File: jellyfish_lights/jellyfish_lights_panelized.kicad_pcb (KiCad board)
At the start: 2 copper layers, 162.8 x 143.6 mm, 424 parts, among them Q1 AO3400A, SW1 tilt switch, U1 SN74LVC1G14DBV

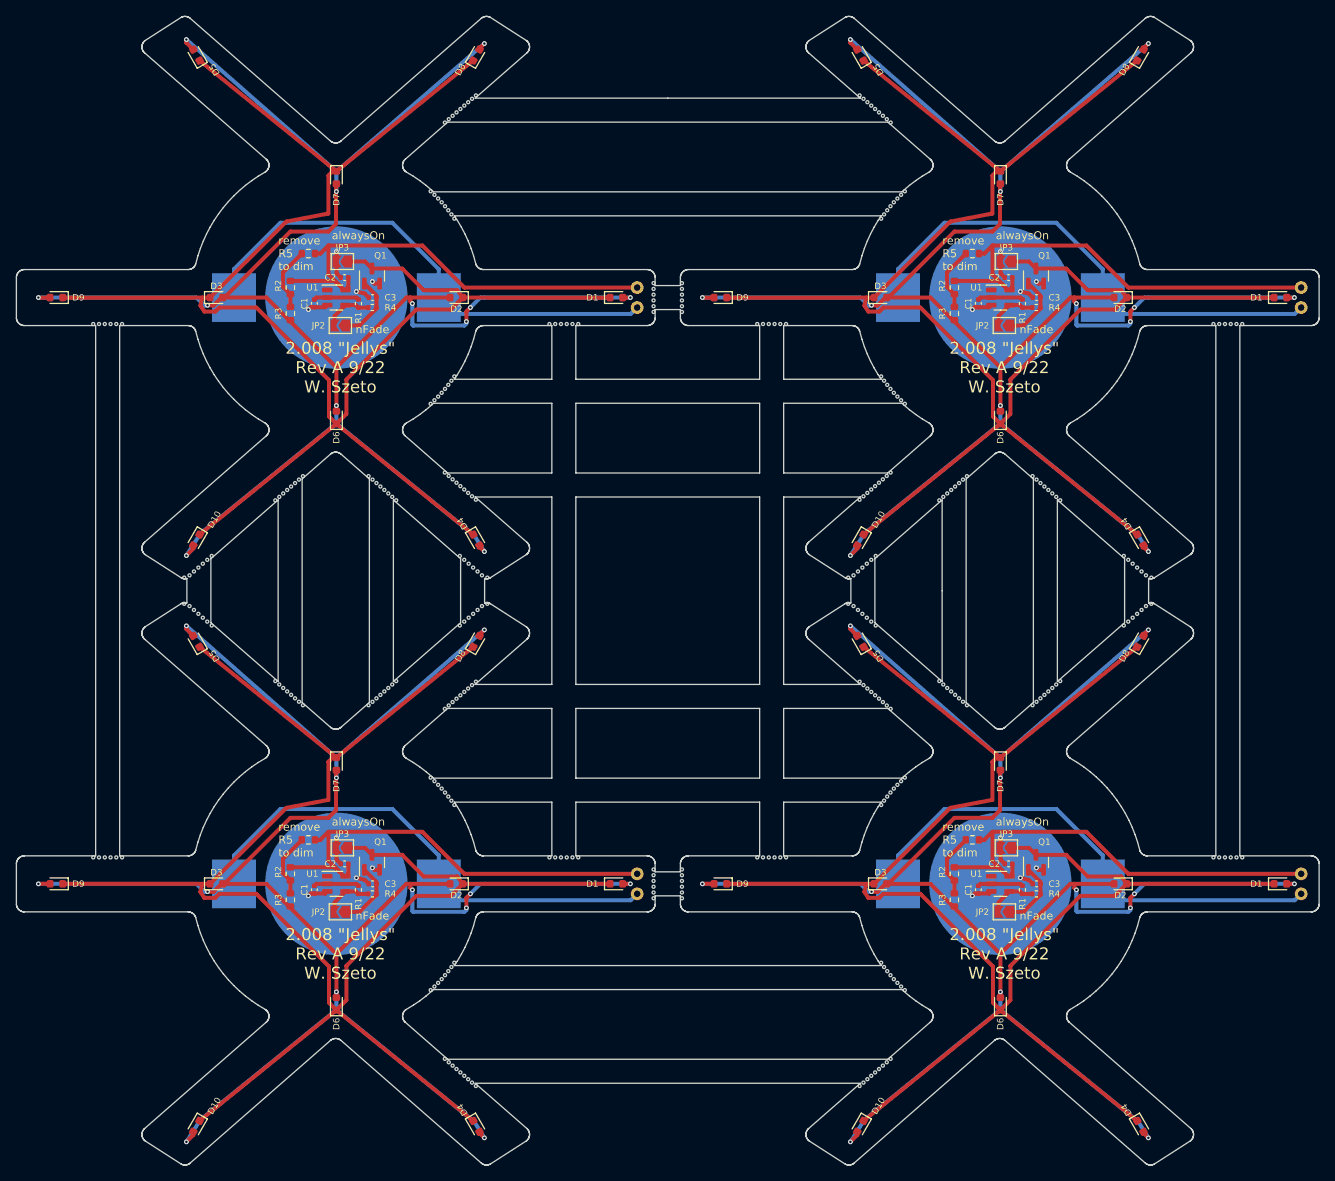
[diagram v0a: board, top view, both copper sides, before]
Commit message: created B01
B01 has a new circuit to do blinking. The op-amp allows for fading of the lights
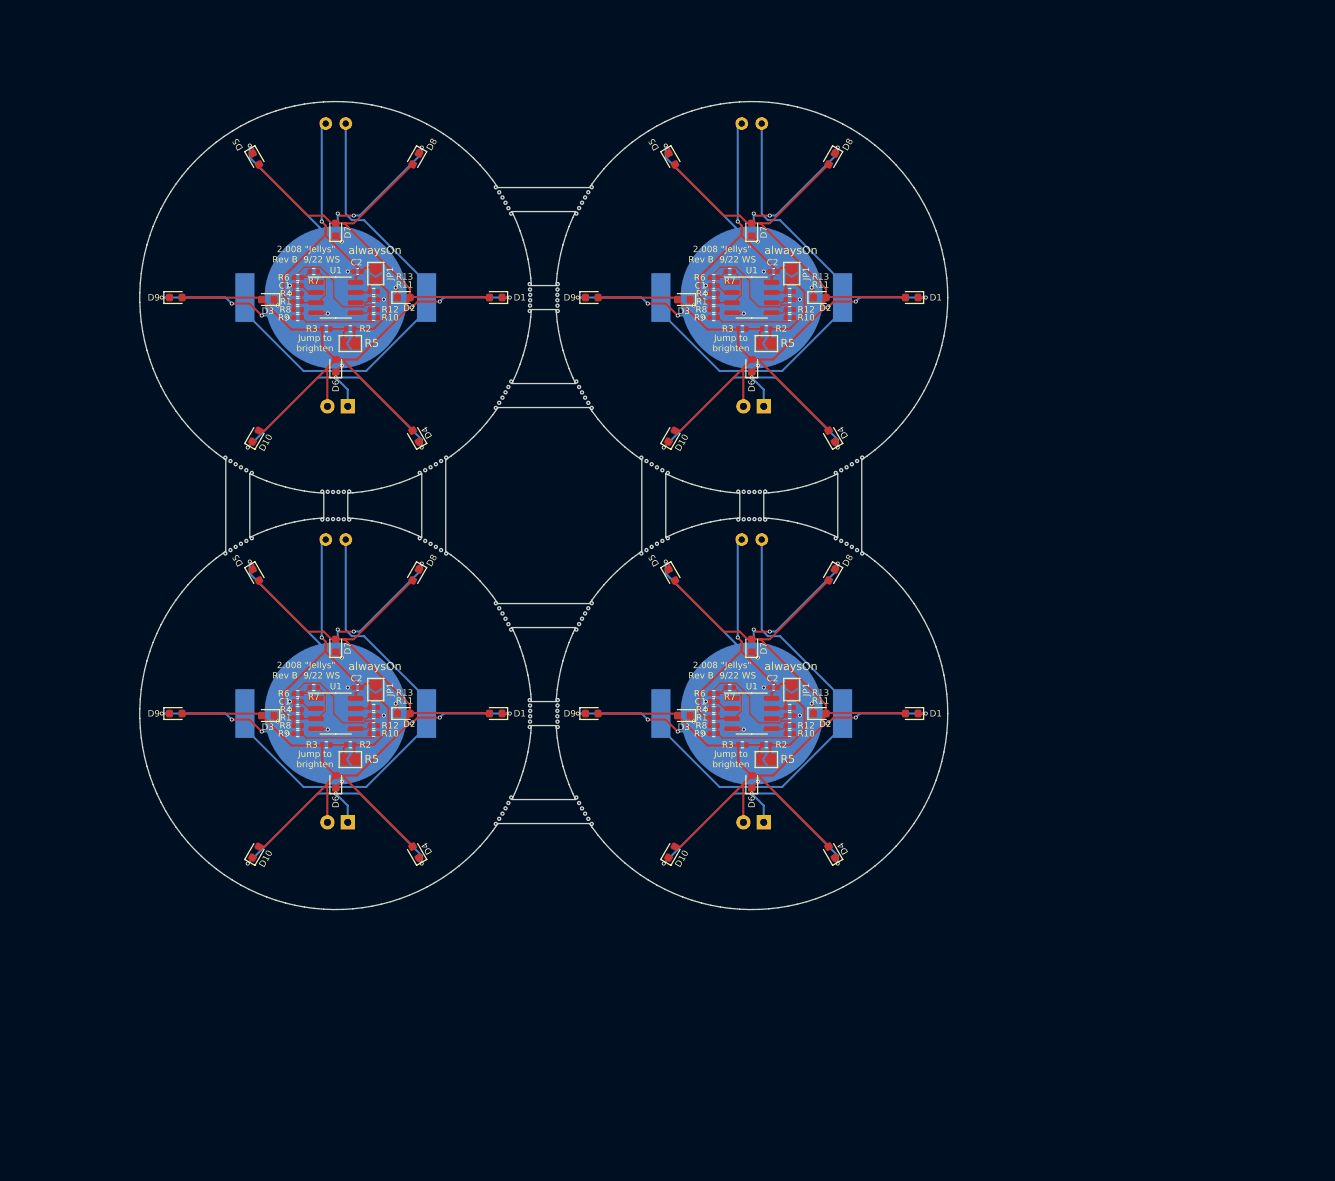
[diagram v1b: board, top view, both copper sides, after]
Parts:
- removed the BT1 at (50.1, 50.0)
- removed the BT1 at (133.1, 123.3)
- removed the BT1 at (133.1, 50.0)
- removed the BT1 at (50.1, 123.3)
- removed the C1 at (47.3, 50.7)
- removed the C1 at (130.3, 50.7)
- removed the C1 at (130.3, 124.0)
- removed the C1 at (47.3, 124.0)
- removed the C2 at (51.1, 120.8)
- removed the C2 at (134.1, 120.8)
- removed the C2 at (134.1, 47.5)
- removed the C2 at (51.1, 47.5)
- removed C3 (x4): 1uF, Capacitor_SMD:C_0402_1005Metric
- removed the D1 at (85.1, 123.3)
- removed the D1 at (168.1, 50.0)
- removed the D1 at (85.1, 50.0)
- removed the D1 at (168.1, 123.3)
- removed the D10 at (32.6, 80.3)
- removed the D10 at (115.6, 80.3)
- removed the D10 at (115.6, 153.6)
- removed the D10 at (32.6, 153.6)
- removed the D2 at (148.1, 50.0)
- removed the D2 at (65.1, 123.3)
- removed the D2 at (148.1, 123.3)
- removed the D2 at (65.1, 50.0)
- removed the D3 at (35.1, 50.0)
- removed the D3 at (118.1, 123.3)
- removed the D3 at (35.1, 123.3)
- removed the D3 at (118.1, 50.0)
- removed the D4 at (67.6, 80.3)
- removed the D4 at (150.6, 80.3)
- removed the D4 at (67.6, 153.6)
- removed the D4 at (150.6, 153.6)
- removed the D5 at (32.6, 19.7)
- removed the D5 at (115.6, 19.7)
- removed the D5 at (32.6, 93.0)
- removed the D5 at (115.6, 93.0)
- removed the D6 at (50.1, 138.3)
- removed the D6 at (133.1, 138.3)
- removed the D6 at (133.1, 65.0)
- removed the D6 at (50.1, 65.0)
- removed the D7 at (133.1, 108.3)
- removed the D7 at (50.1, 108.3)
- removed the D7 at (50.1, 35.0)
- removed the D7 at (133.1, 35.0)
- removed the D8 at (67.6, 93.0)
- removed the D8 at (67.6, 19.7)
- removed the D8 at (150.6, 19.7)
- removed the D8 at (150.6, 93.0)
- removed the D9 at (15.1, 123.3)
- removed the D9 at (98.1, 50.0)
- removed the D9 at (98.1, 123.3)
- removed the D9 at (15.1, 50.0)
- removed JP2 (x4): nFade, Jumper:SolderJumper-2_P1.3mm_Open_TrianglePad1.0x1.5mm
- removed JP3 (x4): alwaysOn, Jumper:SolderJumper-2_P1.3mm_Open_TrianglePad1.0x1.5mm
- removed Q1 (x4): AO3400A, Package_TO_SOT_SMD:SOT-23
- removed the R1 at (52.8, 50.7)
- removed the R1 at (135.8, 50.7)
- removed the R1 at (52.8, 124.0)
- removed the R1 at (135.8, 124.0)
- removed the R2 at (127.3, 122.0)
- removed the R2 at (127.3, 48.7)
- removed the R2 at (44.3, 122.0)
- removed the R2 at (44.3, 48.7)
- removed the R3 at (127.3, 52.0)
- removed the R3 at (44.3, 52.0)
- removed the R3 at (44.3, 125.3)
- removed the R3 at (127.3, 125.3)
- removed the R4 at (137.6, 124.5)
- removed the R4 at (54.6, 124.5)
- removed the R4 at (54.6, 51.2)
- removed the R4 at (137.6, 51.2)
- removed the R5 at (46.6, 44.5)
- removed the R5 at (129.6, 117.8)
- removed the R5 at (46.6, 117.8)
- removed the R5 at (129.6, 44.5)
- removed the REF** at (137.6, 72.8)
- removed the REF** at (128.9, 101.0)
- removed the REF** at (119.3, 111.9)
- removed the REF** at (121.1, 63.3)
- removed the REF** at (150.7, 84.2)
- removed the REF** at (66.6, 25.6)
- removed the REF** at (66.1, 26.0)
- removed the REF** at (118.4, 72.7)
- removed the REF** at (118.9, 72.3)
- removed the REF** at (148.5, 91.0)
- removed the REF** at (66.1, 147.3)
- removed the REF** at (119.3, 134.7)
- removed the REF** at (137.1, 72.3)
- removed the REF** at (138.1, 73.2)
- removed the REF** at (103.4, 53.3)
- removed the REF** at (63.2, 111.4)
- removed the REF** at (161.2, 53.3)
- removed the REF** at (93.3, 48.2)
- removed the REF** at (105.6, 53.3)
- removed the REF** at (56.1, 99.2)
- removed the REF** at (61.9, 36.7)
- removed the REF** at (65.1, 73.1)
- removed the REF** at (31.7, 84.7)
- removed the REF** at (56.6, 74.5)
- removed the REF** at (61.9, 110.0)
- removed the REF** at (62.3, 110.5)
- removed the REF** at (66.1, 99.3)
- removed the REF** at (43.4, 74.5)
- removed the REF** at (125.4, 75.3)
- removed the REF** at (126.9, 74.1)
- removed the REF** at (162.6, 53.3)
- removed the REF** at (45.9, 101.0)
- removed the REF** at (32.8, 89.5)
- removed the REF** at (117.9, 100.1)
- removed the REF** at (64.8, 40.1)
- removed the REF** at (103.4, 120.0)
- removed the REF** at (66.6, 90.0)
- removed the REF** at (119.4, 145.2)
- removed the REF** at (89.7, 122.9)
- removed the REF** at (119.8, 135.2)
- removed the REF** at (67.7, 84.2)
- removed the REF** at (148.5, 82.3)
- removed the REF** at (55.1, 100.1)
- removed the REF** at (116.9, 147.3)
- removed the REF** at (93.3, 121.5)
- removed the REF** at (64.6, 100.6)
- removed the REF** at (89.7, 49.6)
- removed the REF** at (116.4, 83.3)
- removed the REF** at (57.6, 75.3)
- removed the REF** at (128.4, 100.5)
- removed the REF** at (151.3, 84.7)
- removed the REF** at (64.5, 39.6)
- removed the REF** at (126.9, 99.2)
- removed the REF** at (65.1, 146.4)
- removed the REF** at (138.1, 100.1)
- removed the REF** at (61.9, 136.6)
- removed the REF** at (31.1, 88.3)
- removed the REF** at (64.1, 27.7)
- removed the REF** at (118.9, 145.6)
- removed the REF** at (137.6, 100.5)
- removed the REF** at (66.5, 98.9)
- removed the REF** at (63.2, 38.1)
- removed the REF** at (89.7, 125.1)
- removed the REF** at (64.1, 72.3)
- removed the REF** at (119.8, 61.9)
- removed the REF** at (65.6, 26.4)
- removed the REF** at (114.1, 88.3)
- removed the REF** at (63.7, 111.9)
- removed the REF** at (117.4, 146.9)
- removed the REF** at (43.4, 98.8)
- removed the REF** at (140.6, 97.9)
- removed the REF** at (89.7, 51.8)
- removed the REF** at (89.7, 51.1)
- removed the REF** at (55.6, 73.6)
- removed the REF** at (127.4, 73.6)
- removed the REF** at (118.5, 39.6)
- removed the REF** at (43.9, 99.2)
- removed the REF** at (149.1, 90.5)
- removed the REF** at (64.8, 133.1)
- removed the REF** at (106.3, 53.3)
- removed the REF** at (89.7, 48.9)
- removed the REF** at (45.4, 72.8)
- removed the REF** at (93.3, 51.8)
- removed the REF** at (163.3, 53.3)
- removed the REF** at (64.1, 134.2)
- removed the REF** at (119.8, 111.4)
- removed the REF** at (78.2, 53.3)
- removed the REF** at (116.9, 90.5)
- removed the REF** at (21.1, 53.3)
- removed the REF** at (161.2, 120.0)
- removed the REF** at (161.9, 53.3)
- removed the REF** at (120.2, 110.9)
- removed the REF** at (150.2, 89.5)
- removed the REF** at (64.1, 60.9)
- removed the REF** at (80.3, 120.0)
- removed the REF** at (62.8, 37.6)
- removed the REF** at (67.0, 98.4)
- removed the REF** at (118.4, 27.3)
- removed the REF** at (54.1, 72.3)
- removed the REF** at (151.9, 88.3)
- removed the REF** at (89.7, 50.4)
- removed the REF** at (117.5, 82.3)
- removed the REF** at (116.0, 74.8)
- removed the REF** at (44.9, 100.1)
- removed the REF** at (121.1, 110.0)
- removed the REF** at (43.9, 74.1)
- removed the REF** at (105.6, 120.0)
- removed the REF** at (67.5, 98.0)
- removed the REF** at (65.5, 82.3)
- removed the REF** at (64.1, 101.0)
- removed the REF** at (117.9, 26.9)
- removed the REF** at (80.3, 53.3)
- removed the REF** at (76.7, 120.0)
- removed the REF** at (159.7, 120.0)
- removed the REF** at (118.9, 101.0)
- removed the REF** at (159.7, 53.3)
- removed the REF** at (65.1, 26.9)
- removed the REF** at (162.6, 120.0)
- removed the REF** at (67.2, 89.5)
- removed the REF** at (63.7, 61.4)
- removed the REF** at (126.4, 98.8)
- removed the REF** at (139.1, 99.2)
- removed the REF** at (93.3, 125.1)
- removed the REF** at (21.8, 120.0)
- removed the REF** at (68.9, 85.0)
- removed the REF** at (93.3, 49.6)
- removed the REF** at (116.0, 148.1)
- removed the REF** at (119.4, 101.4)
- removed the REF** at (31.7, 88.6)
- removed the REF** at (116.9, 74.0)
- removed the REF** at (115.5, 75.3)
- removed the REF** at (42.4, 75.3)
- removed the REF** at (114.7, 84.7)
- removed the REF** at (118.9, 27.7)
- removed the REF** at (89.7, 121.5)
- removed the REF** at (44.4, 73.6)
- removed the REF** at (149.6, 83.3)
- removed the REF** at (63.6, 101.4)
- removed the REF** at (44.9, 73.2)
- removed the REF** at (118.2, 59.9)
- removed the REF** at (34.5, 91.0)
- removed the REF** at (67.5, 24.7)
- removed the REF** at (42.9, 98.4)
- removed the REF** at (161.9, 120.0)
- removed the REF** at (64.8, 113.4)
- removed the REF** at (63.7, 38.6)
- removed the REF** at (149.1, 82.8)
- removed the REF** at (54.6, 100.5)
- removed the REF** at (67.2, 83.8)
- removed the REF** at (55.6, 99.7)
- removed the REF** at (120.7, 37.2)
- removed the REF** at (21.8, 53.3)
- removed the REF** at (116.0, 25.2)
- removed the REF** at (137.1, 101.0)
- removed the REF** at (32.3, 89.1)
- removed the REF** at (140.1, 74.9)
- removed the REF** at (67.7, 89.1)
- removed the REF** at (115.8, 83.8)
- removed the REF** at (66.6, 83.3)
- removed the REF** at (76.7, 53.3)
- removed the REF** at (139.6, 74.5)
- removed the REF** at (114.7, 88.6)
- removed the REF** at (128.4, 72.8)
- removed the REF** at (120.7, 136.1)
- removed the REF** at (23.3, 120.0)
- removed the REF** at (57.1, 74.9)
- removed the REF** at (63.2, 61.9)
- removed the REF** at (33.4, 83.3)
- removed the REF** at (150.2, 83.8)
- removed the REF** at (139.1, 74.1)
- removed the REF** at (79.6, 120.0)
- removed the REF** at (68.3, 88.6)
- removed the REF** at (104.1, 53.3)
- removed the REF** at (33.4, 90.0)
- removed the REF** at (119.3, 38.6)
- removed the REF** at (117.9, 73.1)
- removed the REF** at (120.2, 37.6)
- removed the REF** at (22.6, 120.0)
- removed the REF** at (65.6, 146.9)
- removed the REF** at (34.5, 82.3)
- removed the REF** at (89.7, 122.2)
- removed the REF** at (117.4, 99.7)
- removed the REF** at (63.6, 28.1)
- removed the REF** at (45.9, 72.3)
- removed the REF** at (117.5, 91.0)
- removed the REF** at (33.9, 90.5)
- removed the REF** at (104.8, 53.3)
- removed the REF** at (64.1, 145.6)
- removed the REF** at (116.9, 82.8)
- removed the REF** at (138.6, 99.7)
- removed the REF** at (57.6, 97.9)
- removed the REF** at (127.4, 99.7)
- removed the REF** at (118.9, 60.9)
- removed the REF** at (66.5, 74.4)
- removed the REF** at (64.5, 133.7)
- removed the REF** at (65.1, 100.1)
- removed the REF** at (63.6, 145.2)
- removed the REF** at (140.1, 98.4)
- removed the REF** at (118.9, 39.1)
- removed the REF** at (89.7, 123.6)
- removed the REF** at (44.4, 99.7)
- removed the REF** at (31.1, 85.0)
- removed the REF** at (140.6, 75.3)
- removed the REF** at (118.9, 134.2)
- removed the REF** at (56.1, 74.1)
- removed the REF** at (77.4, 53.3)
- removed the REF** at (23.3, 53.3)
- removed the REF** at (115.5, 24.7)
- removed the REF** at (116.9, 26.0)
- removed the REF** at (118.4, 146.0)
- removed the REF** at (116.0, 98.4)
- removed the REF** at (89.7, 124.4)
- removed the REF** at (119.3, 61.4)
- removed the REF** at (104.8, 120.0)
- removed the REF** at (104.1, 120.0)
- removed the REF** at (119.4, 28.1)
- removed the REF** at (128.9, 72.3)
- removed the REF** at (116.5, 25.6)
- removed the REF** at (78.9, 120.0)
- removed the REF** at (114.1, 85.0)
- removed the REF** at (102.7, 53.3)
- removed the REF** at (68.9, 88.3)
- removed the REF** at (93.3, 124.4)
- removed the REF** at (163.3, 120.0)
- removed the REF** at (151.9, 85.0)
- removed the REF** at (118.2, 40.1)
- removed the REF** at (118.9, 112.4)
- removed the REF** at (120.2, 62.4)
- removed the REF** at (21.1, 120.0)
- removed the REF** at (116.9, 99.3)
- removed the REF** at (149.6, 90.0)
- removed the REF** at (125.9, 74.9)
- removed the REF** at (32.8, 83.8)
- removed the REF** at (63.7, 134.7)
- removed the REF** at (56.6, 98.8)
- removed the REF** at (151.3, 88.6)
- removed the REF** at (66.1, 82.8)
- removed the REF** at (117.4, 26.4)
- removed the REF** at (115.8, 89.5)
- removed the REF** at (117.4, 73.6)
- removed the REF** at (20.4, 53.3)
- removed the REF** at (150.7, 89.1)
- removed the REF** at (78.2, 120.0)
- removed the REF** at (66.1, 90.5)
- removed the REF** at (19.7, 53.3)
- removed the REF** at (119.8, 38.1)
- removed the REF** at (54.6, 72.8)
- removed the REF** at (66.1, 74.0)
- removed the REF** at (117.9, 146.4)
- removed the REF** at (115.3, 89.1)
- removed the REF** at (127.9, 100.1)
- removed the REF** at (54.1, 101.0)
- removed the REF** at (93.3, 123.6)
- removed the REF** at (93.3, 51.1)
- removed the REF** at (125.4, 97.9)
- removed the REF** at (160.4, 120.0)
- removed the REF** at (126.4, 74.5)
- removed the REF** at (67.0, 74.8)
- removed the REF** at (121.1, 36.7)
- removed the REF** at (120.7, 110.5)
- removed the REF** at (93.3, 122.9)
- removed the REF** at (116.4, 147.7)
- removed the REF** at (118.5, 112.9)
- removed the REF** at (64.8, 59.9)
- removed the REF** at (139.6, 98.8)
- removed the REF** at (19.7, 120.0)
- removed the REF** at (78.9, 53.3)
- removed the REF** at (118.2, 133.1)
- removed the REF** at (118.4, 100.6)
- removed the REF** at (115.5, 148.6)
- removed the REF** at (138.6, 73.6)
- removed the REF** at (22.6, 53.3)
- removed the REF** at (64.1, 112.4)
- removed the REF** at (116.5, 98.9)
- removed the REF** at (121.1, 136.6)
- removed the REF** at (64.6, 27.3)
- removed the REF** at (65.6, 99.7)
- removed the REF** at (115.5, 98.0)
- removed the REF** at (125.9, 98.4)
- removed the REF** at (93.3, 122.2)
- removed the REF** at (62.3, 37.2)
- removed the REF** at (120.7, 62.8)
- removed the REF** at (93.3, 50.4)
- removed the REF** at (65.5, 91.0)
- removed the REF** at (20.4, 120.0)
- removed the REF** at (63.2, 135.2)
- removed the REF** at (55.1, 73.2)
- removed the REF** at (77.4, 120.0)
- removed the REF** at (93.3, 48.9)
- removed the REF** at (64.1, 39.1)
- removed the REF** at (64.6, 72.7)
- removed the REF** at (127.9, 73.2)
- removed the REF** at (67.0, 25.2)
- removed the REF** at (62.3, 136.1)
- removed the REF** at (65.6, 73.6)
- removed the REF** at (45.4, 100.5)
- removed the REF** at (33.9, 82.8)
- removed the REF** at (64.5, 112.9)
- removed the REF** at (106.3, 120.0)
- removed the REF** at (57.1, 98.4)
- removed the REF** at (68.3, 84.7)
- removed the REF** at (118.5, 60.4)
- removed the REF** at (42.4, 97.9)
- removed the REF** at (79.6, 53.3)
- removed the REF** at (64.5, 60.4)
- removed the REF** at (67.5, 75.3)
- removed the REF** at (118.2, 113.4)
- removed the REF** at (67.0, 148.1)
- removed the REF** at (64.6, 146.0)
- removed the REF** at (160.4, 53.3)
- removed the REF** at (116.4, 74.4)
- removed the REF** at (62.8, 110.9)
- removed the REF** at (62.8, 135.7)
- removed the REF** at (89.7, 48.2)
- removed the REF** at (66.6, 147.7)
- removed the REF** at (61.9, 63.3)
- removed the REF** at (118.5, 133.7)
- removed the REF** at (63.6, 71.9)
- removed the REF** at (116.4, 90.0)
- removed the REF** at (120.2, 135.7)
- removed the REF** at (67.5, 148.6)
- removed the REF** at (119.4, 71.9)
- removed the REF** at (32.3, 84.2)
- removed the REF** at (115.3, 84.2)
- removed the REF** at (62.8, 62.4)
- removed the REF** at (62.3, 62.8)
- removed the REF** at (42.9, 74.9)
- removed the REF** at (102.7, 120.0)
- removed the SW1 at (87.7, 122.0)
- removed the SW1 at (87.7, 48.7)
- removed the SW1 at (170.7, 48.7)
- removed the SW1 at (170.7, 122.0)
- removed the U1 at (133.1, 50.0)
- removed the U1 at (133.1, 123.3)
- removed the U1 at (50.1, 50.0)
- removed the U1 at (50.1, 123.3)
- added BT1: Battery_Cell, Battery:BatteryHolder_MPD_BC2003_1x2032, B.Cu at (50.0, 50.0)
- added BT1: Battery_Cell, Battery:BatteryHolder_MPD_BC2003_1x2032, B.Cu at (102.0, 50.0)
- added BT1: Battery_Cell, Battery:BatteryHolder_MPD_BC2003_1x2032, B.Cu at (50.0, 102.0)
- added BT1: Battery_Cell, Battery:BatteryHolder_MPD_BC2003_1x2032, B.Cu at (102.0, 102.0)
- added C1: 10uF, Capacitor_SMD:C_0402_1005Metric, F.Cu at (97.2, 100.5)
- added C1: 10uF, Capacitor_SMD:C_0402_1005Metric, F.Cu at (45.2, 48.5)
- added C1: 10uF, Capacitor_SMD:C_0402_1005Metric, F.Cu at (45.2, 100.5)
- added C1: 10uF, Capacitor_SMD:C_0402_1005Metric, F.Cu at (97.2, 48.5)
- added C2: 100nF, Capacitor_SMD:C_0402_1005Metric, F.Cu at (104.8, 98.8)
- added C2: 100nF, Capacitor_SMD:C_0402_1005Metric, F.Cu at (52.8, 46.8)
- added C2: 100nF, Capacitor_SMD:C_0402_1005Metric, F.Cu at (52.8, 98.8)
- added C2: 100nF, Capacitor_SMD:C_0402_1005Metric, F.Cu at (104.8, 46.8)
- added D1: LED, LED_SMD:LED_0603_1608Metric, F.Cu at (122.0, 102.0)
- added D1: LED, LED_SMD:LED_0603_1608Metric, F.Cu at (122.0, 50.0)
- added D1: LED, LED_SMD:LED_0603_1608Metric, F.Cu at (70.0, 102.0)
- added D1: LED, LED_SMD:LED_0603_1608Metric, F.Cu at (70.0, 50.0)
- added D10: LED, LED_SMD:LED_0603_1608Metric, F.Cu at (40.0, 119.3)
- added D10: LED, LED_SMD:LED_0603_1608Metric, F.Cu at (92.0, 119.3)
- added D10: LED, LED_SMD:LED_0603_1608Metric, F.Cu at (40.0, 67.3)
- added D10: LED, LED_SMD:LED_0603_1608Metric, F.Cu at (92.0, 67.3)
- added D11: LED, LED_THT:LED_D5.0mm, B.Cu at (51.5, 115.6)
- added D11: LED, LED_THT:LED_D5.0mm, B.Cu at (103.5, 63.6)
- added D11: LED, LED_THT:LED_D5.0mm, B.Cu at (51.5, 63.6)
- added D11: LED, LED_THT:LED_D5.0mm, B.Cu at (103.5, 115.6)
- added D2: LED, LED_SMD:LED_0603_1608Metric, F.Cu at (58.5, 50.0)
- added D2: LED, LED_SMD:LED_0603_1608Metric, F.Cu at (110.5, 102.0)
- added D2: LED, LED_SMD:LED_0603_1608Metric, F.Cu at (58.5, 102.0)
- added D2: LED, LED_SMD:LED_0603_1608Metric, F.Cu at (110.5, 50.0)
- added D3: LED, LED_SMD:LED_0603_1608Metric, F.Cu at (41.5, 50.2)
- added D3: LED, LED_SMD:LED_0603_1608Metric, F.Cu at (93.5, 50.2)
- added D3: LED, LED_SMD:LED_0603_1608Metric, F.Cu at (93.5, 102.2)
- added D3: LED, LED_SMD:LED_0603_1608Metric, F.Cu at (41.5, 102.2)
- added D4: LED, LED_SMD:LED_0603_1608Metric, F.Cu at (60.0, 67.3)
- added D4: LED, LED_SMD:LED_0603_1608Metric, F.Cu at (112.0, 67.3)
- added D4: LED, LED_SMD:LED_0603_1608Metric, F.Cu at (112.0, 119.3)
- added D4: LED, LED_SMD:LED_0603_1608Metric, F.Cu at (60.0, 119.3)
- added D5: LED, LED_SMD:LED_0603_1608Metric, F.Cu at (92.0, 84.7)
- added D5: LED, LED_SMD:LED_0603_1608Metric, F.Cu at (40.0, 84.7)
- added D5: LED, LED_SMD:LED_0603_1608Metric, F.Cu at (92.0, 32.7)
- added D5: LED, LED_SMD:LED_0603_1608Metric, F.Cu at (40.0, 32.7)
- added D6: LED, LED_SMD:LED_0603_1608Metric, F.Cu at (102.0, 110.5)
- added D6: LED, LED_SMD:LED_0603_1608Metric, F.Cu at (50.0, 110.5)
- added D6: LED, LED_SMD:LED_0603_1608Metric, F.Cu at (102.0, 58.5)
- added D6: LED, LED_SMD:LED_0603_1608Metric, F.Cu at (50.0, 58.5)
- added D7: LED, LED_SMD:LED_0603_1608Metric, F.Cu at (50.0, 41.5)
- added D7: LED, LED_SMD:LED_0603_1608Metric, F.Cu at (102.0, 41.5)
- added D7: LED, LED_SMD:LED_0603_1608Metric, F.Cu at (102.0, 93.5)
- added D7: LED, LED_SMD:LED_0603_1608Metric, F.Cu at (50.0, 93.5)
- added D8: LED, LED_SMD:LED_0603_1608Metric, F.Cu at (112.0, 84.7)
- added D8: LED, LED_SMD:LED_0603_1608Metric, F.Cu at (112.0, 32.7)
- added D8: LED, LED_SMD:LED_0603_1608Metric, F.Cu at (60.0, 32.7)
- added D8: LED, LED_SMD:LED_0603_1608Metric, F.Cu at (60.0, 84.7)
- added D9: LED, LED_SMD:LED_0603_1608Metric, F.Cu at (82.0, 102.0)
- added D9: LED, LED_SMD:LED_0603_1608Metric, F.Cu at (30.0, 50.0)
- added D9: LED, LED_SMD:LED_0603_1608Metric, F.Cu at (82.0, 50.0)
- added D9: LED, LED_SMD:LED_0603_1608Metric, F.Cu at (30.0, 102.0)
- added JP1: alwaysOn, Jumper:SolderJumper-2_P1.3mm_Open_TrianglePad1.0x1.5mm, F.Cu at (55.0, 47.0)
- added JP1: alwaysOn, Jumper:SolderJumper-2_P1.3mm_Open_TrianglePad1.0x1.5mm, F.Cu at (107.0, 47.0)
- added JP1: alwaysOn, Jumper:SolderJumper-2_P1.3mm_Open_TrianglePad1.0x1.5mm, F.Cu at (55.0, 99.0)
- added JP1: alwaysOn, Jumper:SolderJumper-2_P1.3mm_Open_TrianglePad1.0x1.5mm, F.Cu at (107.0, 99.0)
- added R1: 100K, Resistor_SMD:R_0402_1005Metric, F.Cu at (97.2, 50.5)
- added R1: 100K, Resistor_SMD:R_0402_1005Metric, F.Cu at (45.2, 50.5)
- added R1: 100K, Resistor_SMD:R_0402_1005Metric, F.Cu at (45.2, 102.5)
- added R1: 100K, Resistor_SMD:R_0402_1005Metric, F.Cu at (97.2, 102.5)
- added R10: 100K, Resistor_SMD:R_0402_1005Metric, F.Cu at (54.8, 52.5)
- added R10: 100K, Resistor_SMD:R_0402_1005Metric, F.Cu at (106.8, 52.5)
- added R10: 100K, Resistor_SMD:R_0402_1005Metric, F.Cu at (106.8, 104.5)
- added R10: 100K, Resistor_SMD:R_0402_1005Metric, F.Cu at (54.8, 104.5)
- added R11: 100K, Resistor_SMD:R_0402_1005Metric, F.Cu at (106.8, 50.2)
- added R11: 100K, Resistor_SMD:R_0402_1005Metric, F.Cu at (106.8, 102.2)
- added R11: 100K, Resistor_SMD:R_0402_1005Metric, F.Cu at (54.8, 50.2)
- added R11: 100K, Resistor_SMD:R_0402_1005Metric, F.Cu at (54.8, 102.2)
- added R12: 100K, Resistor_SMD:R_0402_1005Metric, F.Cu at (54.8, 51.5)
- added R12: 100K, Resistor_SMD:R_0402_1005Metric, F.Cu at (54.8, 103.5)
- added R12: 100K, Resistor_SMD:R_0402_1005Metric, F.Cu at (106.8, 51.5)
- added R12: 100K, Resistor_SMD:R_0402_1005Metric, F.Cu at (106.8, 103.5)
- added R13: 100K, Resistor_SMD:R_0402_1005Metric, F.Cu at (106.8, 49.2)
- added R13: 100K, Resistor_SMD:R_0402_1005Metric, F.Cu at (106.8, 101.2)
- added R13: 100K, Resistor_SMD:R_0402_1005Metric, F.Cu at (54.8, 49.2)
- added R13: 100K, Resistor_SMD:R_0402_1005Metric, F.Cu at (54.8, 101.2)
- added R2: 10R, Resistor_SMD:R_0402_1005Metric, F.Cu at (51.8, 105.9)
- added R2: 10R, Resistor_SMD:R_0402_1005Metric, F.Cu at (103.8, 105.9)
- added R2: 10R, Resistor_SMD:R_0402_1005Metric, F.Cu at (51.8, 53.9)
- added R2: 10R, Resistor_SMD:R_0402_1005Metric, F.Cu at (103.8, 53.9)
- added R3: 10R, Resistor_SMD:R_0402_1005Metric, F.Cu at (100.8, 53.9)
- added R3: 10R, Resistor_SMD:R_0402_1005Metric, F.Cu at (48.8, 105.9)
- added R3: 10R, Resistor_SMD:R_0402_1005Metric, F.Cu at (48.8, 53.9)
- added R3: 10R, Resistor_SMD:R_0402_1005Metric, F.Cu at (100.8, 105.9)
- added R4: 100K, Resistor_SMD:R_0402_1005Metric, F.Cu at (45.2, 101.5)
- added R4: 100K, Resistor_SMD:R_0402_1005Metric, F.Cu at (97.2, 49.5)
- added R4: 100K, Resistor_SMD:R_0402_1005Metric, F.Cu at (45.2, 49.5)
- added R4: 100K, Resistor_SMD:R_0402_1005Metric, F.Cu at (97.2, 101.5)
- added R5: 0R, Jumper:SolderJumper-2_P1.3mm_Open_TrianglePad1.0x1.5mm, F.Cu at (51.8, 107.8)
- added R5: 0R, Jumper:SolderJumper-2_P1.3mm_Open_TrianglePad1.0x1.5mm, F.Cu at (103.8, 55.8)
- added R5: 0R, Jumper:SolderJumper-2_P1.3mm_Open_TrianglePad1.0x1.5mm, F.Cu at (103.8, 107.8)
- added R5: 0R, Jumper:SolderJumper-2_P1.3mm_Open_TrianglePad1.0x1.5mm, F.Cu at (51.8, 55.8)
- added R6: 100K, Resistor_SMD:R_0402_1005Metric, F.Cu at (97.2, 47.5)
- added R6: 100K, Resistor_SMD:R_0402_1005Metric, F.Cu at (45.2, 99.5)
- added R6: 100K, Resistor_SMD:R_0402_1005Metric, F.Cu at (97.2, 99.5)
- added R6: 100K, Resistor_SMD:R_0402_1005Metric, F.Cu at (45.2, 47.5)
- added R7: 100K, Resistor_SMD:R_0402_1005Metric, F.Cu at (47.2, 46.8)
- added R7: 100K, Resistor_SMD:R_0402_1005Metric, F.Cu at (99.2, 98.8)
- added R7: 100K, Resistor_SMD:R_0402_1005Metric, F.Cu at (47.2, 98.8)
- added R7: 100K, Resistor_SMD:R_0402_1005Metric, F.Cu at (99.2, 46.8)
- added R8: 10k, Resistor_SMD:R_0402_1005Metric, F.Cu at (45.2, 51.5)
- added R8: 10k, Resistor_SMD:R_0402_1005Metric, F.Cu at (97.2, 51.5)
- added R8: 10k, Resistor_SMD:R_0402_1005Metric, F.Cu at (45.2, 103.5)
- added R8: 10k, Resistor_SMD:R_0402_1005Metric, F.Cu at (97.2, 103.5)
- added R9: 10k, Resistor_SMD:R_0402_1005Metric, F.Cu at (45.2, 104.5)
- added R9: 10k, Resistor_SMD:R_0402_1005Metric, F.Cu at (97.2, 104.5)
- added R9: 10k, Resistor_SMD:R_0402_1005Metric, F.Cu at (45.2, 52.5)
- added R9: 10k, Resistor_SMD:R_0402_1005Metric, F.Cu at (97.2, 52.5)
- added REF**: NPTH, NPTH, F.Cu at (81.6, 63.2)
- added REF**: NPTH, NPTH, F.Cu at (80.1, 39.5)
- added REF**: NPTH, NPTH, F.Cu at (77.7, 51.0)
- added REF**: NPTH, NPTH, F.Cu at (51.7, 74.2)
- added REF**: NPTH, NPTH, F.Cu at (88.2, 82.0)
- added REF**: NPTH, NPTH, F.Cu at (80.1, 112.5)
- added REF**: NPTH, NPTH, F.Cu at (74.3, 101.7)
- added REF**: NPTH, NPTH, F.Cu at (102.3, 74.3)
- added REF**: NPTH, NPTH, F.Cu at (115.2, 81.6)
- added REF**: NPTH, NPTH, F.Cu at (113.9, 71.2)
- added REF**: NPTH, NPTH, F.Cu at (113.2, 71.6)
- added REF**: NPTH, NPTH, F.Cu at (61.2, 71.6)
- added REF**: NPTH, NPTH, F.Cu at (36.2, 70.0)
- added REF**: NPTH, NPTH, F.Cu at (101.7, 74.3)
- added REF**: NPTH, NPTH, F.Cu at (77.7, 102.3)
- added REF**: NPTH, NPTH, F.Cu at (71.2, 113.8)
- added REF**: NPTH, NPTH, F.Cu at (81.2, 89.5)
- added REF**: NPTH, NPTH, F.Cu at (37.5, 81.2)
- added REF**: NPTH, NPTH, F.Cu at (115.8, 70.0)
- added REF**: NPTH, NPTH, F.Cu at (74.3, 103.0)
- added REF**: NPTH, NPTH, F.Cu at (89.5, 70.8)
- added REF**: NPTH, NPTH, F.Cu at (74.2, 48.3)
- added REF**: NPTH, NPTH, F.Cu at (77.8, 100.3)
- added REF**: NPTH, NPTH, F.Cu at (90.8, 80.4)
- added REF**: NPTH, NPTH, F.Cu at (101.0, 77.7)
- added REF**: NPTH, NPTH, F.Cu at (74.3, 101.0)
- added REF**: NPTH, NPTH, F.Cu at (74.2, 103.7)
- added REF**: NPTH, NPTH, F.Cu at (89.5, 81.2)
- added REF**: NPTH, NPTH, F.Cu at (77.7, 101.0)
- added REF**: NPTH, NPTH, F.Cu at (49.7, 77.7)
- added REF**: NPTH, NPTH, F.Cu at (80.4, 90.8)
- added REF**: NPTH, NPTH, F.Cu at (81.6, 36.8)
- added REF**: NPTH, NPTH, F.Cu at (61.2, 80.4)
- added REF**: NPTH, NPTH, F.Cu at (77.7, 49.0)
- added REF**: NPTH, NPTH, F.Cu at (70.8, 114.5)
- added REF**: NPTH, NPTH, F.Cu at (74.3, 102.3)
- added REF**: NPTH, NPTH, F.Cu at (115.2, 70.4)
- added REF**: NPTH, NPTH, F.Cu at (70.8, 89.5)
- added REF**: NPTH, NPTH, F.Cu at (91.5, 80.1)
- added REF**: NPTH, NPTH, F.Cu at (80.1, 91.5)
- added REF**: NPTH, NPTH, F.Cu at (82.0, 63.8)
- added REF**: NPTH, NPTH, F.Cu at (49.7, 74.3)
- added REF**: NPTH, NPTH, F.Cu at (70.0, 36.2)
- added REF**: NPTH, NPTH, F.Cu at (71.2, 38.2)
- added REF**: NPTH, NPTH, F.Cu at (70.4, 88.8)
- added REF**: NPTH, NPTH, F.Cu at (36.2, 82.0)
- added REF**: NPTH, NPTH, F.Cu at (74.3, 50.3)
- added REF**: NPTH, NPTH, F.Cu at (39.5, 71.9)
- added REF**: NPTH, NPTH, F.Cu at (63.8, 82.0)
- added REF**: NPTH, NPTH, F.Cu at (48.3, 74.3)
- added REF**: NPTH, NPTH, F.Cu at (112.5, 71.9)
- added REF**: NPTH, NPTH, F.Cu at (88.8, 70.4)
- added REF**: NPTH, NPTH, F.Cu at (51.7, 77.8)
- added REF**: NPTH, NPTH, F.Cu at (37.5, 70.8)
- added REF**: NPTH, NPTH, F.Cu at (74.3, 49.7)
- added REF**: NPTH, NPTH, F.Cu at (80.4, 38.8)
- added REF**: NPTH, NPTH, F.Cu at (90.1, 80.8)
- added REF**: NPTH, NPTH, F.Cu at (81.6, 115.2)
- added REF**: NPTH, NPTH, F.Cu at (113.9, 80.8)
- added REF**: NPTH, NPTH, F.Cu at (36.8, 81.6)
- added REF**: NPTH, NPTH, F.Cu at (81.6, 88.8)
- added REF**: NPTH, NPTH, F.Cu at (114.5, 81.2)
- added REF**: NPTH, NPTH, F.Cu at (112.5, 80.1)
- added REF**: NPTH, NPTH, F.Cu at (77.7, 103.0)
- added REF**: NPTH, NPTH, F.Cu at (50.3, 74.3)
- added REF**: NPTH, NPTH, F.Cu at (51.0, 74.3)
- added REF**: NPTH, NPTH, F.Cu at (71.6, 90.8)
- added REF**: NPTH, NPTH, F.Cu at (82.0, 115.8)
- added REF**: NPTH, NPTH, F.Cu at (39.5, 80.1)
- added REF**: NPTH, NPTH, F.Cu at (70.8, 62.5)
- added REF**: NPTH, NPTH, F.Cu at (103.7, 77.8)
- added REF**: NPTH, NPTH, F.Cu at (70.4, 63.2)
- added REF**: NPTH, NPTH, F.Cu at (60.5, 80.1)
- added REF**: NPTH, NPTH, F.Cu at (77.8, 48.3)
- added REF**: NPTH, NPTH, F.Cu at (74.2, 100.3)
- added REF**: NPTH, NPTH, F.Cu at (81.2, 114.5)
- added REF**: NPTH, NPTH, F.Cu at (38.8, 71.6)
- added REF**: NPTH, NPTH, F.Cu at (114.5, 70.8)
- added REF**: NPTH, NPTH, F.Cu at (70.4, 36.8)
- added REF**: NPTH, NPTH, F.Cu at (71.6, 61.2)
- added REF**: NPTH, NPTH, F.Cu at (71.9, 60.5)
- added REF**: NPTH, NPTH, F.Cu at (80.8, 61.9)
- added REF**: NPTH, NPTH, F.Cu at (61.9, 71.2)
- added REF**: NPTH, NPTH, F.Cu at (80.4, 61.2)
- added REF**: NPTH, NPTH, F.Cu at (77.7, 50.3)
- added REF**: NPTH, NPTH, F.Cu at (38.1, 71.2)
- added REF**: NPTH, NPTH, F.Cu at (70.4, 115.2)
- added REF**: NPTH, NPTH, F.Cu at (81.2, 37.5)
- added REF**: NPTH, NPTH, F.Cu at (62.5, 81.2)
- added REF**: NPTH, NPTH, F.Cu at (51.0, 77.7)
- added REF**: NPTH, NPTH, F.Cu at (71.9, 39.5)
- added REF**: NPTH, NPTH, F.Cu at (38.1, 80.8)
- added REF**: NPTH, NPTH, F.Cu at (60.5, 71.9)
- added REF**: NPTH, NPTH, F.Cu at (77.8, 103.7)
- added REF**: NPTH, NPTH, F.Cu at (103.7, 74.2)
- added REF**: NPTH, NPTH, F.Cu at (103.0, 74.3)
- added REF**: NPTH, NPTH, F.Cu at (102.3, 77.7)
- added REF**: NPTH, NPTH, F.Cu at (61.9, 80.8)
- added REF**: NPTH, NPTH, F.Cu at (71.2, 61.8)
- added REF**: NPTH, NPTH, F.Cu at (49.0, 74.3)
- added REF**: NPTH, NPTH, F.Cu at (90.1, 71.2)
- added REF**: NPTH, NPTH, F.Cu at (90.8, 71.6)
- added REF**: NPTH, NPTH, F.Cu at (77.7, 101.7)
- added REF**: NPTH, NPTH, F.Cu at (88.8, 81.6)
- added REF**: NPTH, NPTH, F.Cu at (62.5, 70.8)
- added REF**: NPTH, NPTH, F.Cu at (63.2, 81.6)
- added REF**: NPTH, NPTH, F.Cu at (101.7, 77.7)
- added REF**: NPTH, NPTH, F.Cu at (103.0, 77.7)
- added REF**: NPTH, NPTH, F.Cu at (74.3, 49.0)
- added REF**: NPTH, NPTH, F.Cu at (70.8, 37.5)
- added REF**: NPTH, NPTH, F.Cu at (88.2, 70.0)
- added REF**: NPTH, NPTH, F.Cu at (70.0, 63.8)
- added REF**: NPTH, NPTH, F.Cu at (80.8, 113.9)
- added REF**: NPTH, NPTH, F.Cu at (71.2, 90.2)
- added REF**: NPTH, NPTH, F.Cu at (74.3, 51.0)
- added REF**: NPTH, NPTH, F.Cu at (80.8, 90.1)
- added REF**: NPTH, NPTH, F.Cu at (70.0, 115.8)
- added REF**: NPTH, NPTH, F.Cu at (71.9, 91.5)
- added REF**: NPTH, NPTH, F.Cu at (81.2, 62.5)
- added REF**: NPTH, NPTH, F.Cu at (80.8, 38.1)
- added REF**: NPTH, NPTH, F.Cu at (82.0, 36.2)
- added REF**: NPTH, NPTH, F.Cu at (91.5, 71.9)
- added REF**: NPTH, NPTH, F.Cu at (113.2, 80.4)
- added REF**: NPTH, NPTH, F.Cu at (100.3, 74.3)
- added REF**: NPTH, NPTH, F.Cu at (80.1, 60.5)
- added REF**: NPTH, NPTH, F.Cu at (77.7, 49.7)
- added REF**: NPTH, NPTH, F.Cu at (63.2, 70.4)
- added REF**: NPTH, NPTH, F.Cu at (49.0, 77.7)
- added REF**: NPTH, NPTH, F.Cu at (74.2, 51.7)
- added REF**: NPTH, NPTH, F.Cu at (115.8, 82.0)
- added REF**: NPTH, NPTH, F.Cu at (77.8, 51.7)
- added REF**: NPTH, NPTH, F.Cu at (71.9, 112.5)
- added REF**: NPTH, NPTH, F.Cu at (36.8, 70.4)
- added REF**: NPTH, NPTH, F.Cu at (80.4, 113.2)
- added REF**: NPTH, NPTH, F.Cu at (50.3, 77.7)
- added REF**: NPTH, NPTH, F.Cu at (38.8, 80.4)
- added REF**: NPTH, NPTH, F.Cu at (63.8, 70.0)
- added REF**: NPTH, NPTH, F.Cu at (82.0, 88.2)
- added REF**: NPTH, NPTH, F.Cu at (70.0, 88.2)
- added REF**: NPTH, NPTH, F.Cu at (101.0, 74.3)
- added REF**: NPTH, NPTH, F.Cu at (71.6, 38.8)
- added REF**: NPTH, NPTH, F.Cu at (48.3, 77.7)
- added REF**: NPTH, NPTH, F.Cu at (100.3, 77.7)
- added REF**: NPTH, NPTH, F.Cu at (71.6, 113.2)
- added SW1: tilt switch, Capacitor_THT:C_Radial_D6.3mm_H5.0mm_P2.50mm, B.Cu at (100.8, 28.2)
- added SW1: tilt switch, Capacitor_THT:C_Radial_D6.3mm_H5.0mm_P2.50mm, B.Cu at (48.8, 80.2)
- added SW1: tilt switch, Capacitor_THT:C_Radial_D6.3mm_H5.0mm_P2.50mm, B.Cu at (100.8, 80.2)
- added SW1: tilt switch, Capacitor_THT:C_Radial_D6.3mm_H5.0mm_P2.50mm, B.Cu at (48.8, 28.2)
- added U1: MCP6002-xSN, Package_SO:SOIC-8_3.9x4.9mm_P1.27mm, F.Cu at (102.0, 102.0)
- added U1: MCP6002-xSN, Package_SO:SOIC-8_3.9x4.9mm_P1.27mm, F.Cu at (50.0, 50.0)
- added U1: MCP6002-xSN, Package_SO:SOIC-8_3.9x4.9mm_P1.27mm, F.Cu at (102.0, 50.0)
- added U1: MCP6002-xSN, Package_SO:SOIC-8_3.9x4.9mm_P1.27mm, F.Cu at (50.0, 102.0)
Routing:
- net Board_2-Net-(D1-Pad1): track 218.1 -> 0.00 mm
- net Board_3-Net-(D1-Pad1): track 218.1 -> 0.00 mm
- net Board_0-Net-(D1-Pad1): track 218.1 -> 0.00 mm
- net Board_1-Net-(D1-Pad1): track 218.1 -> 0.00 mm
- net Board_3-GND: track 8.83 -> 145.6 mm, vias 4 -> 23
- net Board_2-GND: track 8.83 -> 145.6 mm, vias 4 -> 23
- net Board_1-GND: track 8.83 -> 145.6 mm, vias 4 -> 23
- net Board_0-GND: track 8.83 -> 145.6 mm, vias 4 -> 23
- net Board_3-Net-(D1-Pad2): track 232.7 -> 117.9 mm, vias 12 -> 0
- net Board_1-Net-(D1-Pad2): track 232.7 -> 117.9 mm, vias 12 -> 0
- net Board_0-Net-(D1-Pad2): track 232.7 -> 117.9 mm, vias 12 -> 0
- net Board_2-Net-(D1-Pad2): track 232.7 -> 117.9 mm, vias 12 -> 0
- net Board_1-VCC: track 57.4 -> 37.9 mm, vias 0 -> 1
- net Board_3-VCC: track 57.4 -> 37.9 mm, vias 0 -> 1
- net Board_0-VCC: track 57.4 -> 37.9 mm, vias 0 -> 1
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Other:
- board size 162.8 x 143.6 mm -> 101 x 101 mm
- board text added: "2.008 {dblquote}Jellys{dblquote} Rev B 9/22 WS"
- board text added: "Jump to brighten"
- board text removed: "2.008 {dblquote}Jellys{dblquote} Rev A 9/22 W. Szeto"
- board text removed: "nFade"
- board text removed: "remove R5 to dim"
